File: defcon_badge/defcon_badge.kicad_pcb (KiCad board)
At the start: 4 copper layers, 86 x 54 mm, 79 parts, among them J11 JST-PH 2P, J20 PJ-320A, J30 SAO 2x3, J31 microSD, J32 UART debug, J33 Dev/SWD header, SW1 SS-12D00, SW20 TS-1187A, SW21 TS-1187A, SW22 TS-1187A, U10 TP4056, U11 ME6211C33M5G, U2 W25Q16JVUXIQ, U20 TM8211, U21 TDA1308, U3 RP2040, U30 TSOP4838, Y1 ABM8-272-T3

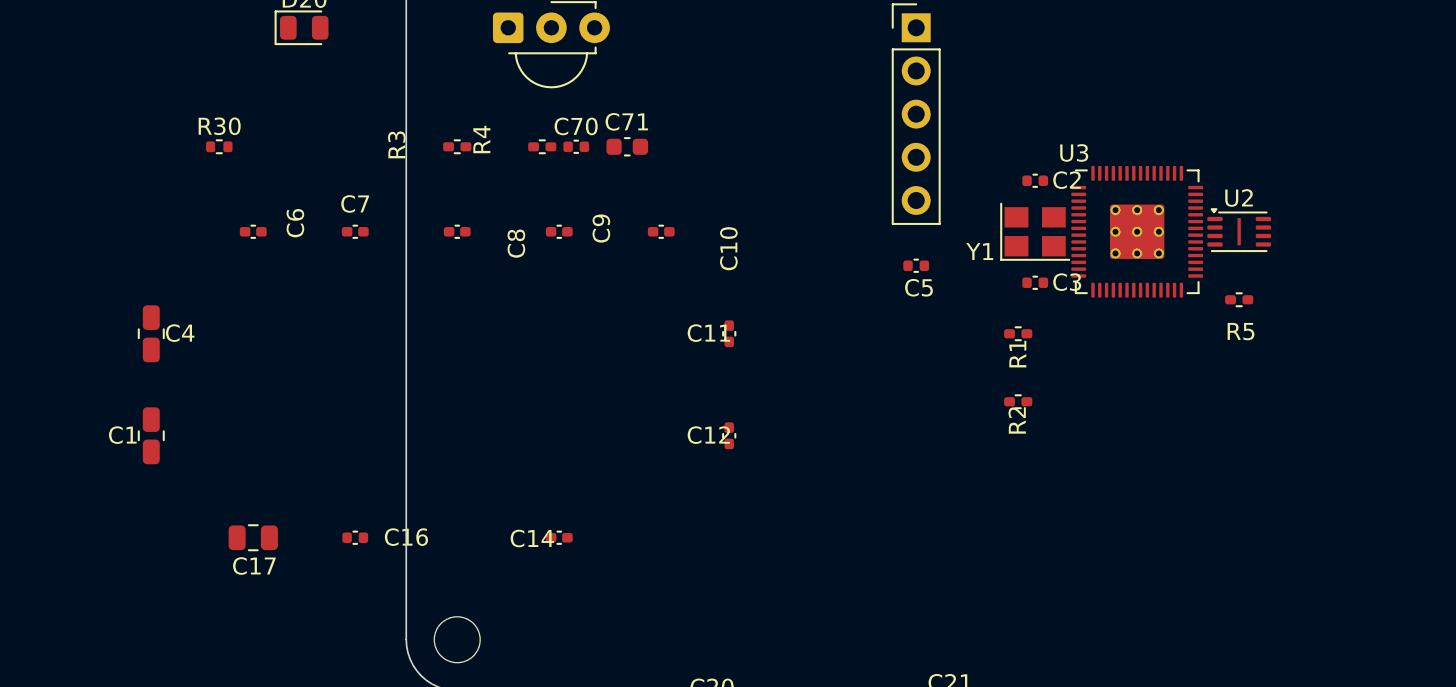
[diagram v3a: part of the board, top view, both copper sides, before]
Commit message: iter(4): decoupling caps around RP2040
13 caps (C1, C4, C5-C12, C14, C16, C17) now form a tight ring around U3.
100n at y=102 (above QFN) and y=112 (below QFN), 1u at y=115 outer row,
10u bulk at y=118. All within board bounds, on the center MCU zone.

Co-Authored-By: Claude Opus 4.7 (1M context) <noreply@anthropic.com>
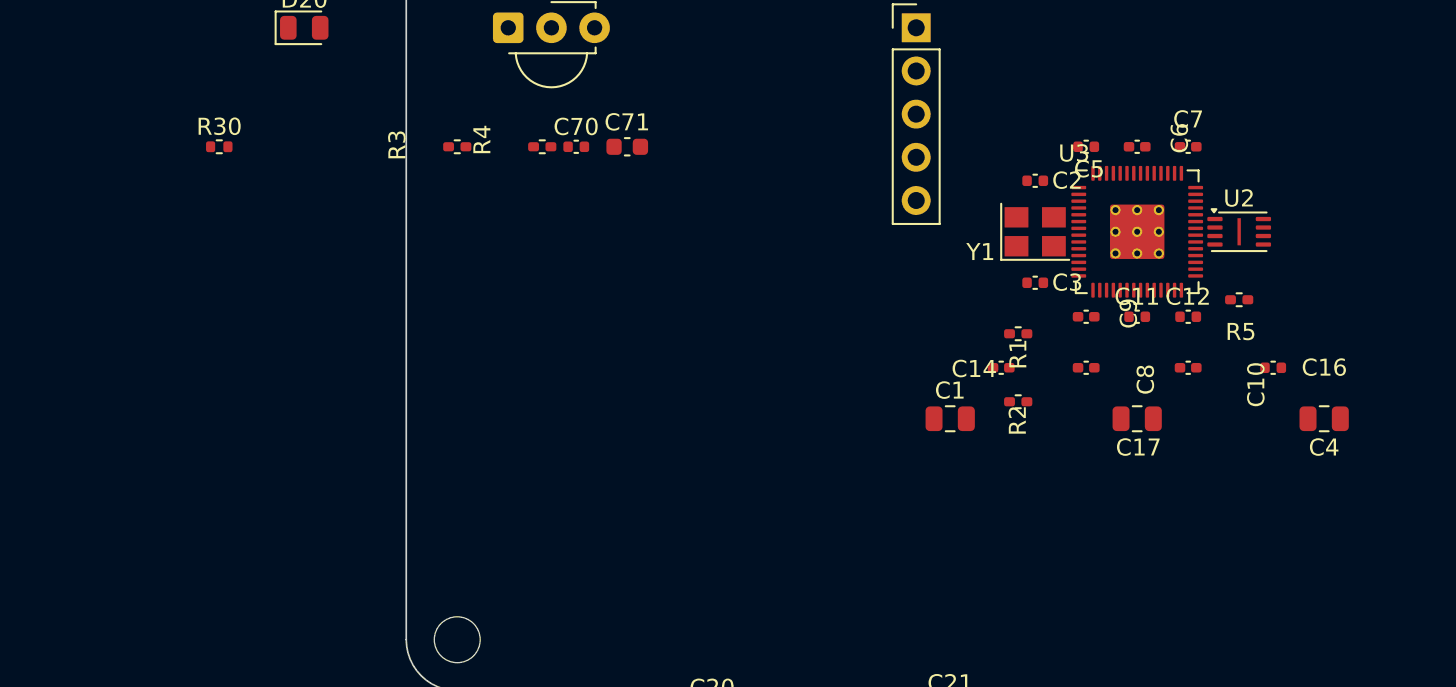
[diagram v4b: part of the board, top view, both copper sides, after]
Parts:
- moved C4 69.2 mm to (154.0, 118.0), turned to 0 degrees
- moved C16 54.9 mm to (151.0, 115.0)
- moved C17 52.5 mm to (143.0, 118.0)
- moved C6 52.2 mm to (143.0, 102.0)
- moved C7 49.3 mm to (146.0, 102.0)
- moved C1 47.0 mm to (132.0, 118.0), turned to 0 degrees
- moved C8 37.9 mm to (140.0, 115.0)
- moved C10 32.0 mm to (146.0, 115.0)
- moved C9 31.4 mm to (140.0, 112.0)
- moved C12 27.9 mm to (146.0, 112.0), turned to 0 degrees
- moved C14 27.9 mm to (135.0, 115.0)
- moved C11 24.0 mm to (143.0, 112.0), turned to 0 degrees
- moved C5 12.2 mm to (140.0, 102.0)
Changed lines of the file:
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@@
 	(footprint "Capacitor_SMD:C_0805_2012Metric"
 		(layer "B.Cu")
-		(at 85 113 90)
+		(at 154.000 118.000)
 		(descr "Capacitor SMD 0805 (2012 Metric), square (rectangular) end terminal, IPC_7351 nominal, (Body size source: IPC-SM-782 page 76, https://www.pcb-3d.com/wordpress/wp-content/uploads/ipc-sm-782a_amendment_1_and_2.pdf, https://docs.google.com/spreadsheets/d/1BsfQQcO9C6DZCsRaXUlFlo91Tg2WpOkGARC1WS5S8t0/edit?usp=sharing), generated with kicad-footprint-generator")
 		(tags "capacitor")
@@
 	(footprint "Capacitor_SMD:C_0402_1005Metric"
 		(layer "B.Cu")
-		(at 115 107)
+		(at 146.000 115.000)
 		(descr "Capacitor SMD 0402 (1005 Metric), square (rectangular) end terminal, IPC_7351 nominal, (Body size source: IPC-SM-782 page 76, https://www.pcb-3d.com/wordpress/wp-content/uploads/ipc-sm-782a_amendment_1_and_2.pdf), generated with kicad-footprint-generator")
 		(tags "capacitor")
@@
 	(footprint "Capacitor_SMD:C_0402_1005Metric"
 		(layer "B.Cu")
-		(at 103 107)
+		(at 140.000 115.000)
 		(descr "Capacitor SMD 0402 (1005 Metric), square (rectangular) end terminal, IPC_7351 nominal, (Body size source: IPC-SM-782 page 76, https://www.pcb-3d.com/wordpress/wp-content/uploads/ipc-sm-782a_amendment_1_and_2.pdf), generated with kicad-footprint-generator")
 		(tags "capacitor")
@@
 	(footprint "Capacitor_SMD:C_0402_1005Metric"
 		(layer "B.Cu")
-		(at 130 109)
+		(at 140.000 102.000)
 		(descr "Capacitor SMD 0402 (1005 Metric), square (rectangular) end terminal, IPC_7351 nominal, (Body size source: IPC-SM-782 page 76, https://www.pcb-3d.com/wordpress/wp-content/uploads/ipc-sm-782a_amendment_1_and_2.pdf), generated with kicad-footprint-generator")
 		(tags "capacitor")
@@
 	(footprint "Capacitor_SMD:C_0402_1005Metric"
 		(layer "B.Cu")
-		(at 109 107)
+		(at 140.000 112.000)
 		(descr "Capacitor SMD 0402 (1005 Metric), square (rectangular) end terminal, IPC_7351 nominal, (Body size source: IPC-SM-782 page 76, https://www.pcb-3d.com/wordpress/wp-content/uploads/ipc-sm-782a_amendment_1_and_2.pdf), generated with kicad-footprint-generator")
 		(tags "capacitor")
@@
 	(footprint "Capacitor_SMD:C_0402_1005Metric"
 		(layer "B.Cu")
-		(at 119 119 90)
+		(at 146.000 112.000)
 		(descr "Capacitor SMD 0402 (1005 Metric), square (rectangular) end terminal, IPC_7351 nominal, (Body size source: IPC-SM-782 page 76, https://www.pcb-3d.com/wordpress/wp-content/uploads/ipc-sm-782a_amendment_1_and_2.pdf), generated with kicad-footprint-generator")
 		(tags "capacitor")
@@
 	(footprint "Capacitor_SMD:C_0402_1005Metric"
 		(layer "B.Cu")
-		(at 109 125)
+		(at 135.000 115.000)
 		(descr "Capacitor SMD 0402 (1005 Metric), square (rectangular) end terminal, IPC_7351 nominal, (Body size source: IPC-SM-782 page 76, https://www.pcb-3d.com/wordpress/wp-content/uploads/ipc-sm-782a_amendment_1_and_2.pdf), generated with kicad-footprint-generator")
 		(tags "capacitor")
@@
 	(footprint "Capacitor_SMD:C_0402_1005Metric"
 		(layer "B.Cu")
-		(at 97 107)
+		(at 146.000 102.000)
 		(descr "Capacitor SMD 0402 (1005 Metric), square (rectangular) end terminal, IPC_7351 nominal, (Body size source: IPC-SM-782 page 76, https://www.pcb-3d.com/wordpress/wp-content/uploads/ipc-sm-782a_amendment_1_and_2.pdf), generated with kicad-footprint-generator")
 		(tags "capacitor")
@@
 	(footprint "Capacitor_SMD:C_0805_2012Metric"
 		(layer "B.Cu")
-		(at 85 119 90)
+		(at 132.000 118.000)
 		(descr "Capacitor SMD 0805 (2012 Metric), square (rectangular) end terminal, IPC_7351 nominal, (Body size source: IPC-SM-782 page 76, https://www.pcb-3d.com/wordpress/wp-content/uploads/ipc-sm-782a_amendment_1_and_2.pdf, https://docs.google.com/spreadsheets/d/1BsfQQcO9C6DZCsRaXUlFlo91Tg2WpOkGARC1WS5S8t0/edit?usp=sharing), generated with kicad-footprint-generator")
 		(tags "capacitor")
@@
 	(footprint "Capacitor_SMD:C_0402_1005Metric"
 		(layer "B.Cu")
-		(at 119 113 90)
+		(at 143.000 112.000)
 		(descr "Capacitor SMD 0402 (1005 Metric), square (rectangular) end terminal, IPC_7351 nominal, (Body size source: IPC-SM-782 page 76, https://www.pcb-3d.com/wordpress/wp-content/uploads/ipc-sm-782a_amendment_1_and_2.pdf), generated with kicad-footprint-generator")
 		(tags "capacitor")
@@
 	(footprint "Capacitor_SMD:C_0402_1005Metric"
 		(layer "B.Cu")
-		(at 97 125)
+		(at 151.000 115.000)
 		(descr "Capacitor SMD 0402 (1005 Metric), square (rectangular) end terminal, IPC_7351 nominal, (Body size source: IPC-SM-782 page 76, https://www.pcb-3d.com/wordpress/wp-content/uploads/ipc-sm-782a_amendment_1_and_2.pdf), generated with kicad-footprint-generator")
 		(tags "capacitor")
@@
 	(footprint "Capacitor_SMD:C_0402_1005Metric"
 		(layer "B.Cu")
-		(at 91 107)
+		(at 143.000 102.000)
 		(descr "Capacitor SMD 0402 (1005 Metric), square (rectangular) end terminal, IPC_7351 nominal, (Body size source: IPC-SM-782 page 76, https://www.pcb-3d.com/wordpress/wp-content/uploads/ipc-sm-782a_amendment_1_and_2.pdf), generated with kicad-footprint-generator")
 		(tags "capacitor")
@@
 	(footprint "Capacitor_SMD:C_0805_2012Metric"
 		(layer "B.Cu")
-		(at 91 125)
+		(at 143.000 118.000)
 		(descr "Capacitor SMD 0805 (2012 Metric), square (rectangular) end terminal, IPC_7351 nominal, (Body size source: IPC-SM-782 page 76, https://www.pcb-3d.com/wordpress/wp-content/uploads/ipc-sm-782a_amendment_1_and_2.pdf, https://docs.google.com/spreadsheets/d/1BsfQQcO9C6DZCsRaXUlFlo91Tg2WpOkGARC1WS5S8t0/edit?usp=sharing), generated with kicad-footprint-generator")
 		(tags "capacitor")

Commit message: iter(5): LED strip across top edge
LED20-23 SK9822 5x5mm placed at y=92 with 20mm pitch starting at x=113.
Each LED has a 10n bypass cap (C60-C63) at y=96 immediately below it.
Known conflict: LED20 grazes U30 TSOP IR receiver and LED21 crowds J33
SWD header. Iter 6 will relocate U30/D20/J33/R3/R4/R30 out of the LED row.

Co-Authored-By: Claude Opus 4.7 (1M context) <noreply@anthropic.com>
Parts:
- moved LED20 48.1 mm to (113.0, 92.0)
- moved C60 47.1 mm to (113.0, 96.0)
- moved LED21 46.2 mm to (133.0, 92.0)
- moved C61 45.2 mm to (133.0, 96.0)
- moved LED22 44.4 mm to (153.0, 92.0)
- moved C62 43.3 mm to (153.0, 96.0)
- moved LED23 42.5 mm to (173.0, 92.0)
- moved C63 41.4 mm to (173.0, 96.0)
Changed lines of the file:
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@@
 	(footprint "LED_SMD:LED_SK6812_PLCC4_5.0x5.0mm_P3.2mm"
 		(layer "F.Cu")
-		(at 134 75)
+		(at 173.000 92.000)
 		(descr "5.0mm x 5.0mm Addressable RGB LED NeoPixel, https://cdn-shop.adafruit.com/product-files/1138/SK6812+LED+datasheet+.pdf")
 		(tags "LED RGB NeoPixel PLCC-4 5050")
@@
 	(footprint "Capacitor_SMD:C_0402_1005Metric"
 		(layer "B.Cu")
-		(at 90 82)
+		(at 133.000 96.000)
 		(descr "Capacitor SMD 0402 (1005 Metric), square (rectangular) end terminal, IPC-7351 nominal, (Body size source: IPC-SM-782 page 76, https://www.pcb-3d.com/wordpress/wp-content/uploads/ipc-sm-782a_amendment_1_and_2.pdf)")
 		(tags "capacitor")
@@
 	(footprint "LED_SMD:LED_SK6812_PLCC4_5.0x5.0mm_P3.2mm"
 		(layer "F.Cu")
-		(at 68 75)
+		(at 113.000 92.000)
 		(descr "5.0mm x 5.0mm Addressable RGB LED NeoPixel, https://cdn-shop.adafruit.com/product-files/1138/SK6812+LED+datasheet+.pdf")
 		(tags "LED RGB NeoPixel PLCC-4 5050")
@@
 	(footprint "Capacitor_SMD:C_0402_1005Metric"
 		(layer "B.Cu")
-		(at 112 82)
+		(at 153.000 96.000)
 		(descr "Capacitor SMD 0402 (1005 Metric), square (rectangular) end terminal, IPC-7351 nominal, (Body size source: IPC-SM-782 page 76, https://www.pcb-3d.com/wordpress/wp-content/uploads/ipc-sm-782a_amendment_1_and_2.pdf)")
 		(tags "capacitor")
@@
 	(footprint "Capacitor_SMD:C_0402_1005Metric"
 		(layer "B.Cu")
-		(at 68 82)
+		(at 113.000 96.000)
 		(descr "Capacitor SMD 0402 (1005 Metric), square (rectangular) end terminal, IPC-7351 nominal, (Body size source: IPC-SM-782 page 76, https://www.pcb-3d.com/wordpress/wp-content/uploads/ipc-sm-782a_amendment_1_and_2.pdf)")
 		(tags "capacitor")
@@
 	(footprint "Capacitor_SMD:C_0402_1005Metric"
 		(layer "B.Cu")
-		(at 134 82)
+		(at 173.000 96.000)
 		(descr "Capacitor SMD 0402 (1005 Metric), square (rectangular) end terminal, IPC-7351 nominal, (Body size source: IPC-SM-782 page 76, https://www.pcb-3d.com/wordpress/wp-content/uploads/ipc-sm-782a_amendment_1_and_2.pdf)")
 		(tags "capacitor")
@@
 	(footprint "LED_SMD:LED_SK6812_PLCC4_5.0x5.0mm_P3.2mm"
 		(layer "F.Cu")
-		(at 90 75)
+		(at 133.000 92.000)
 		(descr "5.0mm x 5.0mm Addressable RGB LED NeoPixel, https://cdn-shop.adafruit.com/product-files/1138/SK6812+LED+datasheet+.pdf")
 		(tags "LED RGB NeoPixel PLCC-4 5050")
@@
 	(footprint "LED_SMD:LED_SK6812_PLCC4_5.0x5.0mm_P3.2mm"
 		(layer "F.Cu")
-		(at 112 75)
+		(at 153.000 92.000)
 		(descr "5.0mm x 5.0mm Addressable RGB LED NeoPixel, https://cdn-shop.adafruit.com/product-files/1138/SK6812+LED+datasheet+.pdf")
 		(tags "LED RGB NeoPixel PLCC-4 5050")

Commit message: iter(6): clear LED-row collisions
- U30 TSOP4838 + D20 IR LED + R30 -> bottom center (y=127), facing
  outward off the bottom edge.
- J33 Dev/SWD 1x05 header -> right edge at (180,115), vertical.
- R3/R4 27R USB termination -> left of Y1 crystal at x=133.

LED row is now visually clean across the top edge with no collisions.

Co-Authored-By: Claude Opus 4.7 (1M context) <noreply@anthropic.com>
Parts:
- moved D20 65.4 mm to (151.0, 127.0)
- moved R30 63.2 mm to (147.0, 127.0)
- moved J33 53.9 mm to (180.0, 115.0)
- moved U30 43.2 mm to (135.0, 127.0), turned to 180 degrees
- moved R3 30.1 mm to (133.0, 105.0)
- moved R4 26.2 mm to (133.0, 110.0)
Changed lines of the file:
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@@
 	(footprint "Resistor_SMD:R_0402_1005Metric"
 		(layer "B.Cu")
-		(at 103 102)
+		(at 133.000 105.000)
 		(descr "Resistor SMD 0402 (1005 Metric), square (rectangular) end terminal, IPC_7351 nominal, (Body size source: IPC-SM-782 page 72, https://www.pcb-3d.com/wordpress/wp-content/uploads/ipc-sm-782a_amendment_1_and_2.pdf), generated with kicad-footprint-generator")
 		(tags "resistor")
@@
 	(footprint "Resistor_SMD:R_0402_1005Metric"
 		(layer "B.Cu")
-		(at 108 102)
+		(at 133.000 110.000)
 		(descr "Resistor SMD 0402 (1005 Metric), square (rectangular) end terminal, IPC_7351 nominal, (Body size source: IPC-SM-782 page 72, https://www.pcb-3d.com/wordpress/wp-content/uploads/ipc-sm-782a_amendment_1_and_2.pdf), generated with kicad-footprint-generator")
 		(tags "resistor")
@@
 	(footprint "Resistor_SMD:R_0402_1005Metric"
 		(layer "B.Cu")
-		(at 89 102)
+		(at 147.000 127.000)
 		(descr "Resistor SMD 0402 (1005 Metric), square (rectangular) end terminal, IPC-7351 nominal, (Body size source: IPC-SM-782 page 72, https://www.pcb-3d.com/wordpress/wp-content/uploads/ipc-sm-782a_amendment_1_and_2.pdf)")
 		(tags "resistor")
@@
 	(footprint "OptoDevice:Vishay_MINICAST-3Pin"
 		(layer "F.Cu")
-		(at 106 95)
+		(at 135.000 127.000 180)
 		(descr "IR Receiver Vishay TSOP-xxxx, MINICAST package, see https://www.vishay.com/docs/82669/tsop32s40f.pdf")
 		(tags "IR Receiver Vishay TSOP-xxxx MINICAST")
@@
 	(footprint "LED_SMD:LED_0805_2012Metric"
 		(layer "F.Cu")
-		(at 94 95)
+		(at 151.000 127.000)
 		(descr "LED SMD 0805 (2012 Metric), square (rectangular) end terminal, IPC-7351 nominal, (Body size source: https://docs.google.com/spreadsheets/d/1BsfQQcO9C6DZCsRaXUlFlo91Tg2WpOkGARC1WS5S8t0/edit?usp=sharing)")
 		(tags "LED")
@@
 	(footprint "Connector_PinHeader_2.54mm:PinHeader_1x05_P2.54mm_Vertical"
 		(layer "B.Cu")
-		(at 130 95)
+		(at 180.000 115.000)
 		(descr "Through hole straight pin header, 1x05, 2.54mm pitch, single row")
 		(tags "Through hole pin header THT 1x05 2.54mm single row")
